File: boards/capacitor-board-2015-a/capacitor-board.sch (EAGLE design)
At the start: 13 parts, among them Q1 FDV303N, Q2 FQT1N80

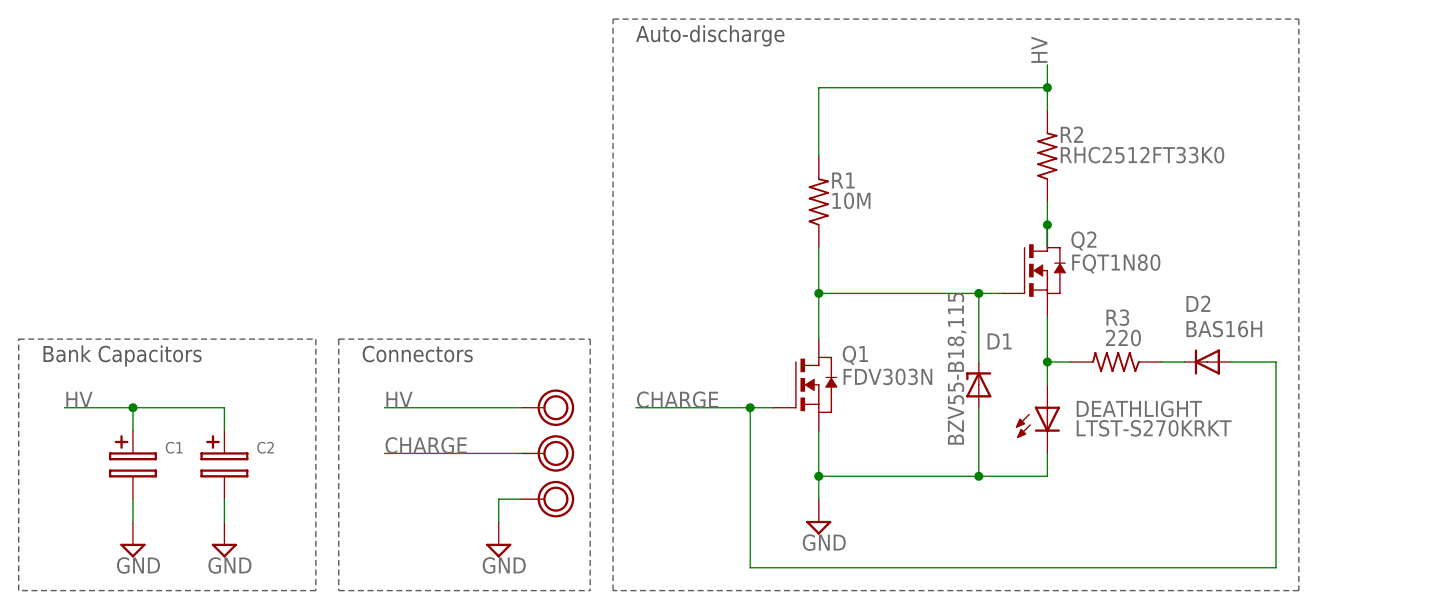
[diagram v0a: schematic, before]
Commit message: capacitor-board-2015-b to capacitor-board-2015-a
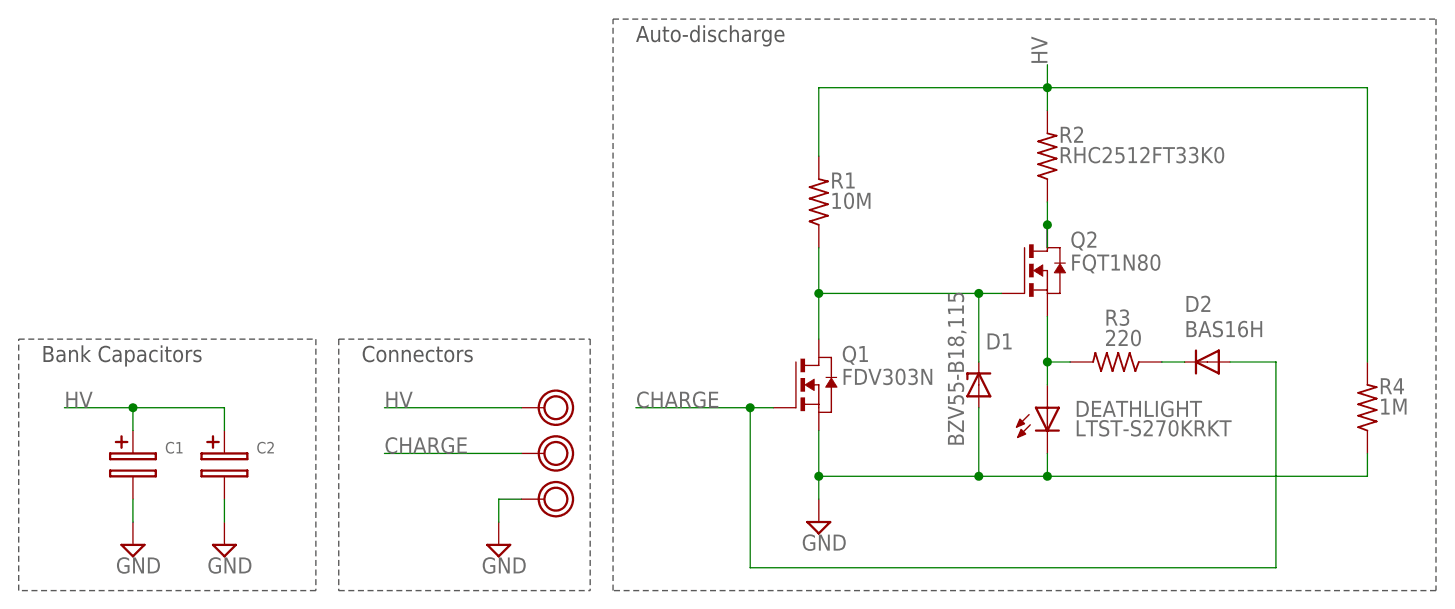
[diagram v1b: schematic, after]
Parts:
- added R4: 1M, rcl:R-US_R0603
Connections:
- net GND: now also R4.1
- net HV: now also R4.2
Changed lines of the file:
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@@
 <part name="R3" library="rcl" deviceset="R-US_" device="R0603" value="220"/>
 <part name="D2" library="diode" deviceset="DIODE-" device="SOD323-W" value="BAS16H"/>
+<part name="R4" library="rcl" deviceset="R-US_" device="R0603" value="1M"/>
 </parts>
 <sheets>
@@
 <wire x1="35.56" y1="27.94" x2="63.5" y2="27.94" width="0.1524" layer="97" style="shortdash"/>
 <text x="38.1" y="25.4" size="1.778" layer="97">Connectors</text>
-<wire x1="66.04" y1="63.5" x2="142.24" y2="63.5" width="0.1524" layer="97" style="shortdash"/>
-<wire x1="142.24" y1="63.5" x2="142.24" y2="0" width="0.1524" layer="97" style="shortdash"/>
-<wire x1="142.24" y1="0" x2="66.04" y2="0" width="0.1524" layer="97" style="shortdash"/>
+<wire x1="66.04" y1="63.5" x2="157.48" y2="63.5" width="0.1524" layer="97" style="shortdash"/>
+<wire x1="157.48" y1="63.5" x2="157.48" y2="0" width="0.1524" layer="97" style="shortdash"/>
+<wire x1="157.48" y1="0" x2="66.04" y2="0" width="0.1524" layer="97" style="shortdash"/>
 <wire x1="66.04" y1="0" x2="66.04" y2="63.5" width="0.1524" layer="97" style="shortdash"/>
 <text x="68.58" y="60.96" size="1.778" layer="97">Auto-discharge</text>
@@
 <attribute name="VALUE" x="129.54" y="28.1686" size="1.778" layer="96"/>
 </instance>
+<instance part="R4" gate="G$1" x="149.86" y="20.32" smashed="yes" rot="R90">
+<attribute name="NAME" x="151.13" y="21.8186" size="1.778" layer="95"/>
+<attribute name="VALUE" x="151.13" y="19.558" size="1.778" layer="96"/>
+</instance>
 </instances>
 <busses>
@@
 <wire x1="114.3" y1="12.7" x2="106.68" y2="12.7" width="0.1524" layer="91"/>
 <junction x="106.68" y="12.7"/>
+<pinref part="R4" gate="G$1" pin="1"/>
+<wire x1="114.3" y1="12.7" x2="149.86" y2="12.7" width="0.1524" layer="91"/>
+<wire x1="149.86" y1="12.7" x2="149.86" y2="15.24" width="0.1524" layer="91"/>
+<junction x="114.3" y="12.7"/>
 </segment>
 </net>
@@
 <pinref part="R1" gate="G$1" pin="2"/>
 <junction x="114.3" y="55.88"/>
+<pinref part="R4" gate="G$1" pin="2"/>
+<wire x1="114.3" y1="55.88" x2="149.86" y2="55.88" width="0.1524" layer="91"/>
+<wire x1="149.86" y1="55.88" x2="149.86" y2="25.4" width="0.1524" layer="91"/>
 </segment>
 </net>
